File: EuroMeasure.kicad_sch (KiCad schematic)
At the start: 47 parts, among them SW1 RESET, SW2 ADR, U1 AMS1117-3.3, U2 STM32G030CxT, Y1 NX2520 16MHz

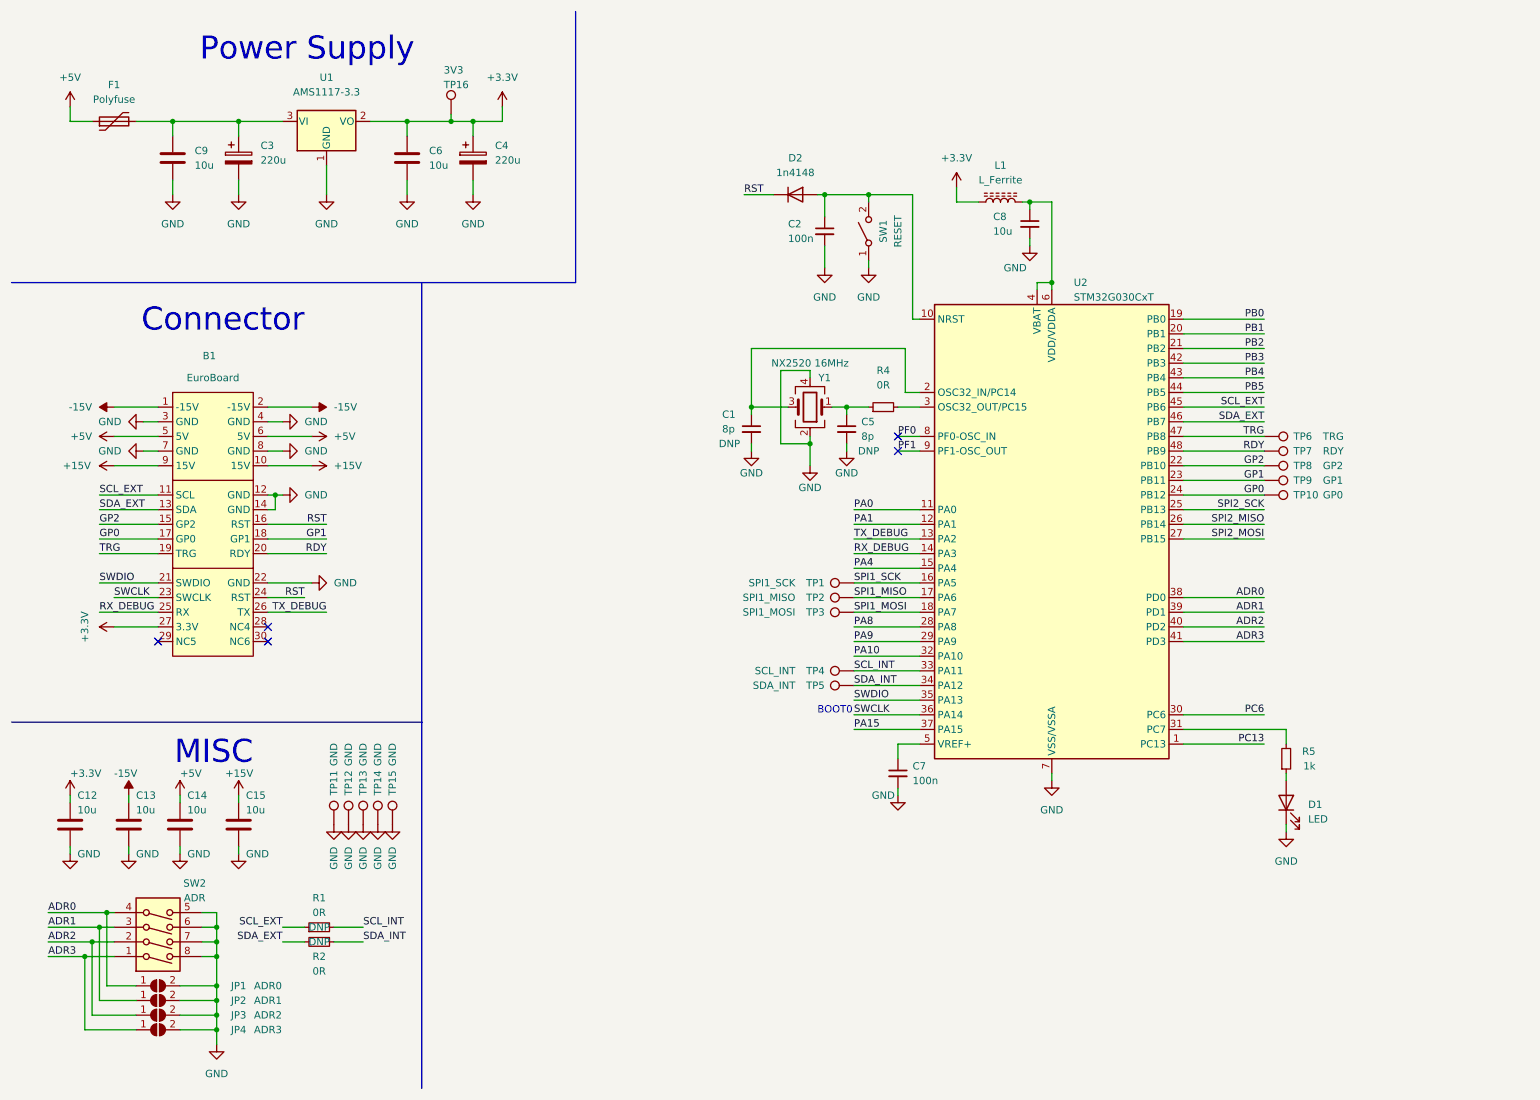
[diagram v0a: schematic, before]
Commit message: Fixed xtal connection
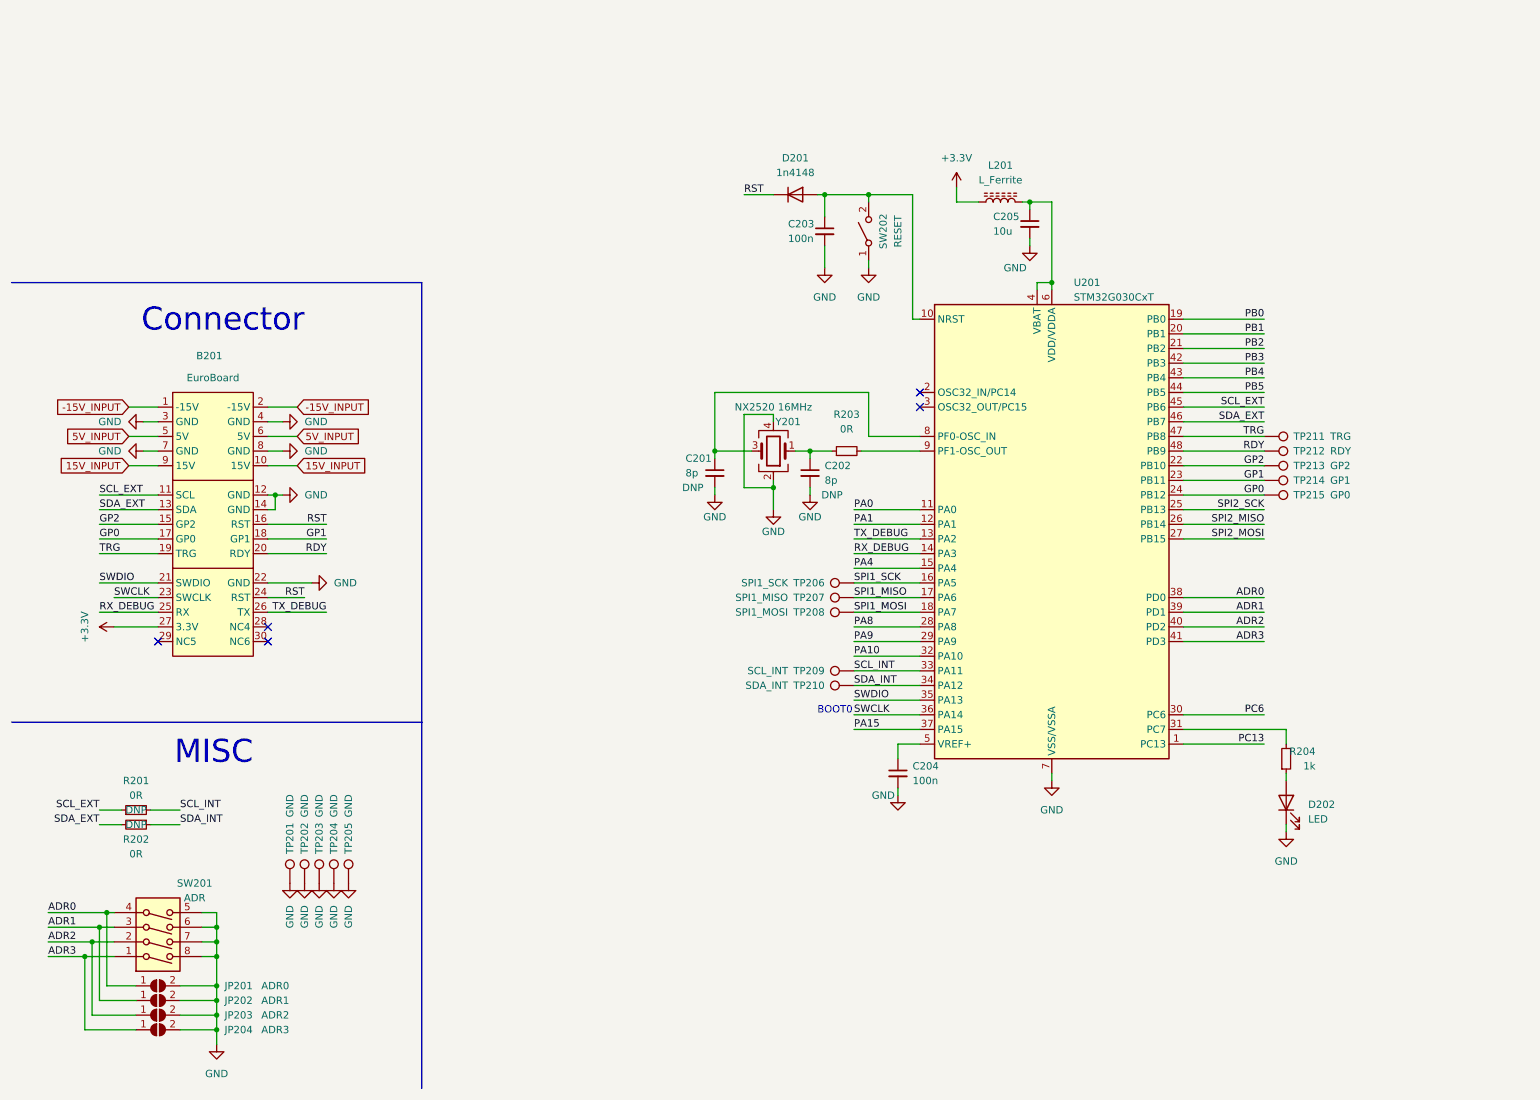
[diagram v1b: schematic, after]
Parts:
- removed C12, C13, C14, C15, C6, C9: 10u, Capacitor_SMD:C_0805_2012Metric_Pad1.18x1.45mm_HandSolder, symbol Device:C
- removed C3, C4: 220u, Capacitor_SMD:CP_Elec_6.3x7.7, symbol Device:C_Polarized
- removed F1: Polyfuse, Fuse:Fuse_1210_3225Metric, symbol Device:Polyfuse
- removed TP16: 3V3, MEMS_Custom:TestPoint_Pad_D1.0mm, symbol Connector:TestPoint
- removed U1: AMS1117-3.3, Package_TO_SOT_SMD:SOT-223-3_TabPin2, symbol Regulator_Linear:AMS1117-3.3
- renumbered B1 to B201, C1 to C201, C5 to C202, C2 to C203, C7 to C204, C8 to C205, D2 to D201, D1 to D202, JP1 to JP201, JP2 to JP202, JP3 to JP203, JP4 to JP204, L1 to L201, R1 to R201, R2 to R202, R4 to R203, R5 to R204, SW2 to SW201, SW1 to SW202, TP11 to TP201, TP12 to TP202, TP13 to TP203, TP14 to TP204, TP15 to TP205, TP1 to TP206, TP2 to TP207, TP3 to TP208, TP4 to TP209, TP5 to TP210, TP6 to TP211, TP7 to TP212, TP8 to TP213, TP9 to TP214, TP10 to TP215, U2 to U201, Y1 to Y201
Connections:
- net PF0 is gone; now on an unnamed net: U201.8 (PF0-OSC_IN)
- net at C201.1, Y201.3: no longer U201.2 (OSC32_IN/PC14)
- net at U201.3 (OSC32_OUT/PC15): no longer R203.2
- net +15V renamed 15V_INPUT
- net +5V renamed 5V_INPUT
- net -15V renamed -15V_INPUT
- net PF1: no longer names the net of U201.9 (PF1-OSC_OUT)
- net PF1: now also R203.2
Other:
- note removed: "Power Supply"
- moved on the sheet: C201, C202, R201, R202, R203, TP201, TP202, TP203, TP204, TP205, Y201

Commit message: Fixed programmer reset
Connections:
- net RST: no longer B201.24 (RST)
- net LOCAL_RST: now reaches C203.1, D201.2 (A), SW202.2 (B), U201.10 (NRST)
- net LOCAL_RST: now also B201.24 (RST)

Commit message: Updated euroboard footprint to accept lockout
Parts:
- TP213: value GP2 -> ~{LOCKOUT}
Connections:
- net GP2 renamed ~{LOCKOUT}
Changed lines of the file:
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@@
     (effects (font (size 1.27 1.27)) (justify left bottom))
   )
-  (label "GP2" (at 26.67 100.33 0) (fields_autoplaced)
+  (label "~{LOCKOUT}" (at 26.67 100.33 0) (fields_autoplaced)
     (effects (font (size 1.27 1.27)) (justify left bottom))
   )
@@
     (effects (font (size 1.27 1.27)) (justify right bottom))
   )
-  (label "GP2" (at 228.6 90.17 180) (fields_autoplaced)
+  (label "~{LOCKOUT}" (at 228.6 90.17 180) (fields_autoplaced)
     (effects (font (size 1.27 1.27)) (justify right bottom))
   )
@@
       (effects (font (size 1.27 1.27)) (justify left))
     )
-    (property "Value" "GP2" (at 240.03 90.17 90)
-      (effects (font (size 1.27 1.27)) (justify left))
-    )
+    (property "Value" "~{LOCKOUT}" (at 240.03 90.17 90)
+      (effects (font (size 1.27 1.27)) (justify left))
+    )

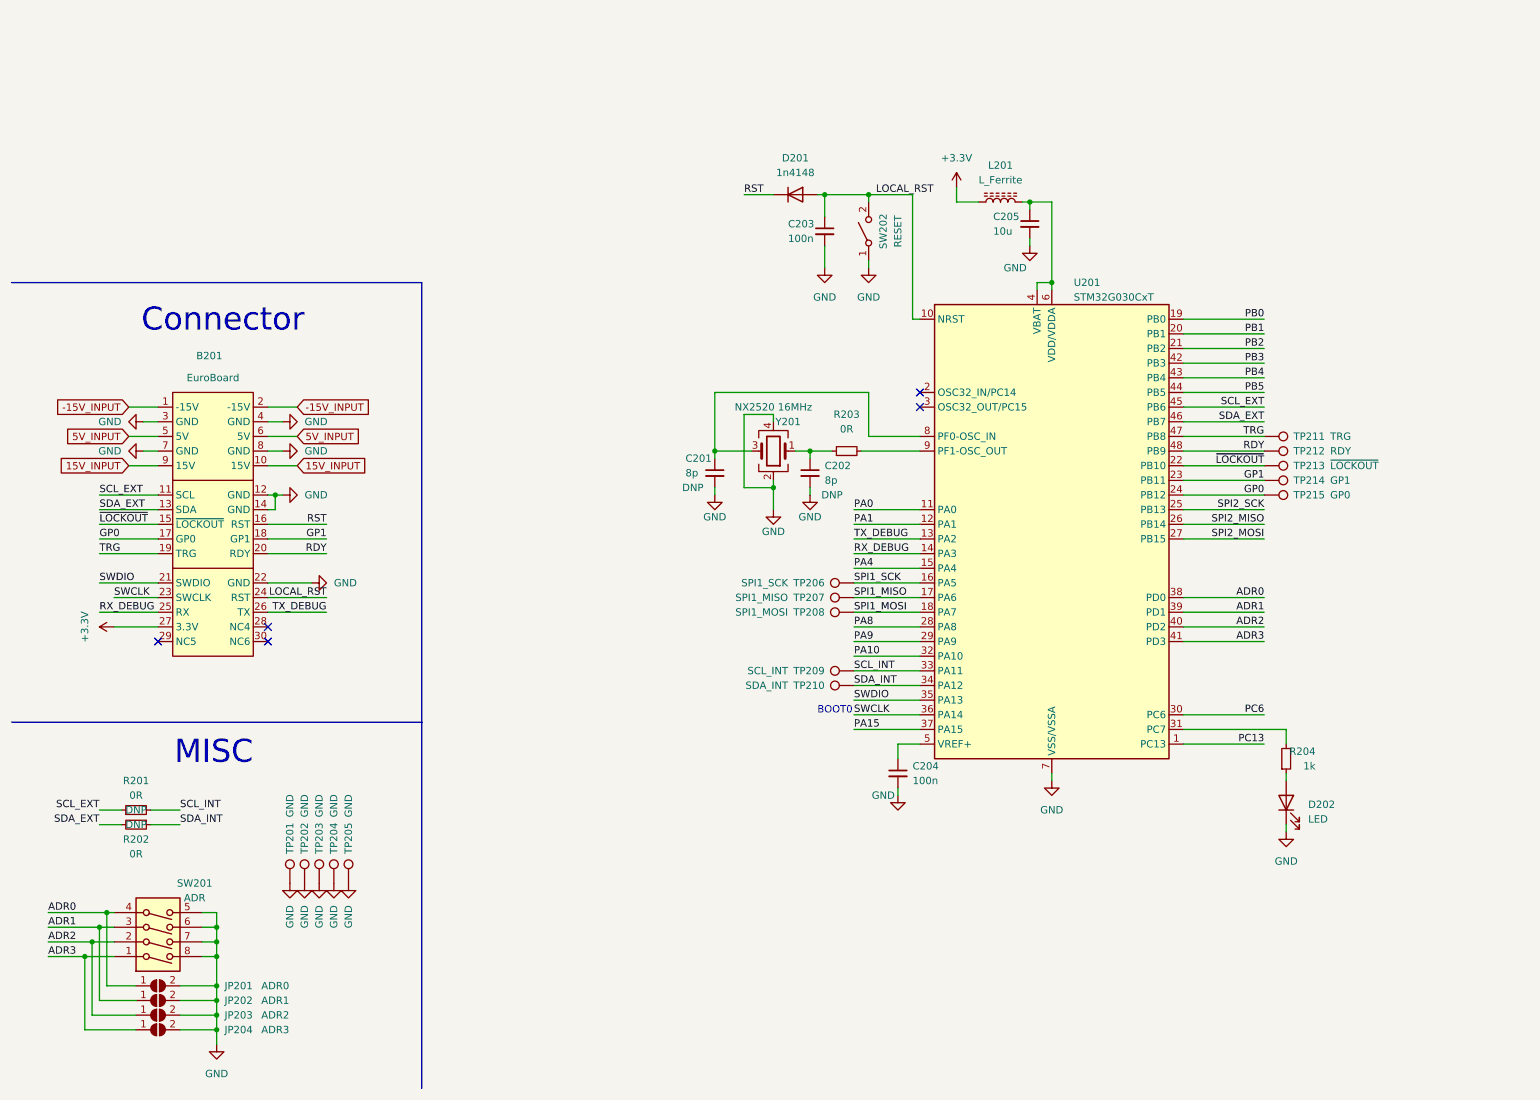
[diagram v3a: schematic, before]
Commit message: Converted for use as the single EuroMeasure.sch file
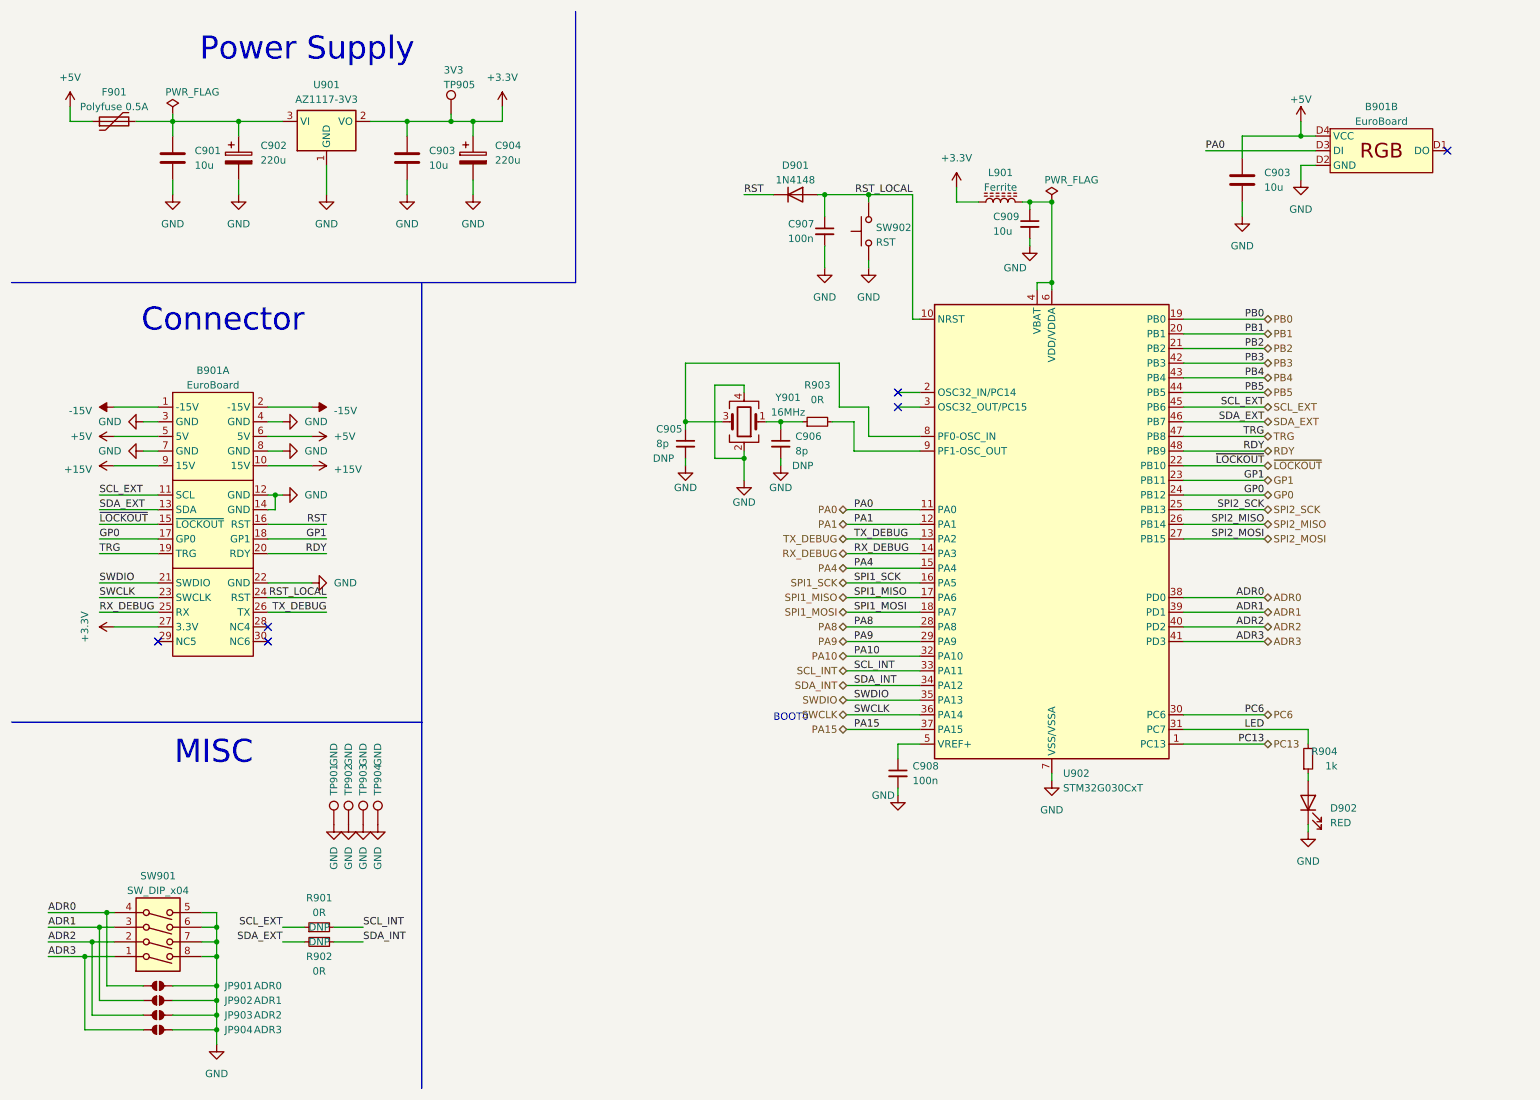
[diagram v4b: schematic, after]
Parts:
- removed B201: EuroBoard, MEMS_Custom:EuroMeasure, symbol MEMS_Custom:EuroBoard
- removed C201, C202: 8p, Capacitor_SMD:C_0805_2012Metric_Pad1.18x1.45mm_HandSolder, symbol Device:C_Small
- removed C203, C204: 100n, Capacitor_SMD:C_0805_2012Metric_Pad1.18x1.45mm_HandSolder, symbol Device:C_Small
- removed C205: 10u, Capacitor_SMD:C_0805_2012Metric_Pad1.18x1.45mm_HandSolder, symbol Device:C_Small
- removed D201: 1n4148, Diode_SMD:D_SOD-123, symbol Device:D
- removed D202: LED, LED_SMD:LED_0805_2012Metric_Pad1.15x1.40mm_HandSolder, symbol Device:LED
- removed JP201: ADR0, MEMS_Passive:R_0805_2012Metric_Jumper, symbol Jumper:SolderJumper_2_Open
- removed JP202: ADR1, MEMS_Passive:R_0805_2012Metric_Jumper, symbol Jumper:SolderJumper_2_Open
- removed JP203: ADR2, MEMS_Passive:R_0805_2012Metric_Jumper, symbol Jumper:SolderJumper_2_Open
- removed JP204: ADR3, MEMS_Passive:R_0805_2012Metric_Jumper, symbol Jumper:SolderJumper_2_Open
- removed L201: L_Ferrite, Inductor_SMD:L_0805_2012Metric_Pad1.15x1.40mm_HandSolder, symbol Device:L_Ferrite
- removed R201, R202, R203: 0R, Capacitor_SMD:C_0805_2012Metric_Pad1.18x1.45mm_HandSolder, symbol Device:R_Small
- removed R204: 1k, Resistor_SMD:R_0805_2012Metric_Pad1.20x1.40mm_HandSolder, symbol Device:R_Small
- removed SW201: ADR, Button_Switch_SMD:SW_DIP_SPSTx04_Slide_Omron_A6H-4101_W6.15mm_P1.27mm, symbol Switch:SW_DIP_x04
- removed SW202: RESET, Button_Switch_SMD:SW_SPST_B3S-1000, symbol Switch:SW_SPST
- removed TP201, TP202, TP203, TP204, TP205: GND, MEMS_Custom:TestPoint_Pad_D1.0mm, symbol Connector:TestPoint
- removed TP206: SPI1_SCK, MEMS_Custom:TestPoint_Pad_D1.0mm, symbol Connector:TestPoint
- removed TP207: SPI1_MISO, MEMS_Custom:TestPoint_Pad_D1.0mm, symbol Connector:TestPoint
- removed TP208: SPI1_MOSI, MEMS_Custom:TestPoint_Pad_D1.0mm, symbol Connector:TestPoint
- removed TP209: SCL_INT, MEMS_Custom:TestPoint_Pad_D1.0mm, symbol Connector:TestPoint
- removed TP210: SDA_INT, MEMS_Custom:TestPoint_Pad_D1.0mm, symbol Connector:TestPoint
- removed TP211: TRG, MEMS_Custom:TestPoint_Pad_D1.0mm, symbol Connector:TestPoint
- removed TP212: RDY, MEMS_Custom:TestPoint_Pad_D1.0mm, symbol Connector:TestPoint
- removed TP213: ~{LOCKOUT}, MEMS_Custom:TestPoint_Pad_D1.0mm, symbol Connector:TestPoint
- removed TP214: GP1, MEMS_Custom:TestPoint_Pad_D1.0mm, symbol Connector:TestPoint
- removed TP215: GP0, MEMS_Custom:TestPoint_Pad_D1.0mm, symbol Connector:TestPoint
- removed U201: STM32G030CxT, Package_QFP:LQFP-48_7x7mm_P0.5mm, symbol MEMS_IC:STM32G030CxT
- removed Y201: NX2520 16MHz, Oscillator:Oscillator_SMD_Abracon_ASDMB-4Pin_2.5x2.0mm, symbol Device:Crystal_GND24
- added B901: EuroBoard, MEMS_Custom:EuroMeasureLED, symbol MEMS_Custom:EuroBoardLED
- added C901, C903 (x2): 10u, Capacitor_SMD:C_0805_2012Metric_Pad1.18x1.45mm_HandSolder, symbol Device:C
- added C902, C904: 220u, Capacitor_SMD:CP_Elec_6.3x7.7, symbol Device:C_Polarized
- added C905, C906: 8p, Capacitor_SMD:C_0805_2012Metric_Pad1.18x1.45mm_HandSolder, symbol Device:C_Small
- added C907, C908: 100n, Capacitor_SMD:C_0805_2012Metric_Pad1.18x1.45mm_HandSolder, symbol Device:C_Small
- added C909: 10u, Capacitor_SMD:C_0805_2012Metric_Pad1.18x1.45mm_HandSolder, symbol Device:C_Small
- added D901: 1N4148, Diode_SMD:D_SOD-323F, symbol MEMS_Discrete-semiconductor:D_1N4148WS-SOD323
- added D902: RED, LED_SMD:LED_0805_2012Metric_Pad1.15x1.40mm_HandSolder, symbol MEMS_Discrete-semiconductor:LED_0805_Red
- added F901: Polyfuse 0.5A, Fuse:Fuse_1210_3225Metric, symbol MEMS_Protection:Polyfuse-500mA-1206L050/15YR
- added JP901: ADR0, MEMS_Passive:R_0805_2012Metric_Jumper, symbol MEMS_Passive:SolderableJumper
- added JP902: ADR1, MEMS_Passive:R_0805_2012Metric_Jumper, symbol MEMS_Passive:SolderableJumper
- added JP903: ADR2, MEMS_Passive:R_0805_2012Metric_Jumper, symbol MEMS_Passive:SolderableJumper
- added JP904: ADR3, MEMS_Passive:R_0805_2012Metric_Jumper, symbol MEMS_Passive:SolderableJumper
- added L901: Ferrite, Inductor_SMD:L_0805_2012Metric_Pad1.15x1.40mm_HandSolder, symbol MEMS_Passive:L_Ferrite_742792040
- added R901, R902, R903: 0R, Capacitor_SMD:C_0805_2012Metric_Pad1.18x1.45mm_HandSolder, symbol Device:R_Small
- added R904: 1k, Resistor_SMD:R_0805_2012Metric_Pad1.20x1.40mm_HandSolder, symbol Device:R_Small
- added SW901: SW_DIP_x04, Button_Switch_SMD:SW_DIP_SPSTx04_Slide_Omron_A6H-4101_W6.15mm_P1.27mm, symbol MEMS_Electromechanical:SW_DIP_A6H-4101
- added SW902: RST, Button_Switch_SMD:SW_SPST_B3S-1000, symbol MEMS_Electromechanical:SW_Push_Tact_B3S-1000
- added TP901, TP902, TP903, TP904: GND, MEMS_Custom:TestPoint_Pad_D1.0mm, symbol Connector:TestPoint
- added TP905: 3V3, MEMS_Custom:TestPoint_Pad_D1.0mm, symbol Connector:TestPoint
- added U901: AZ1117-3V3, Package_TO_SOT_SMD:SOT-223-3_TabPin2, symbol MEMS_IC:AZ1117IH-3.3TRG1-SOT223
- added U902: STM32G030CxT, Package_QFP:LQFP-48_7x7mm_P0.5mm, symbol MEMS_IC:STM32G030CxT
- added Y901: 16MHz, Oscillator:Oscillator_SMD_Abracon_ASDMB-4Pin_2.5x2.0mm, symbol MEMS_Passive:Crystal_16MHz_ECS-160-8-36CKM-TR3
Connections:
- net +3.3V: now also B901.27 (3.3V), C903.1, C904.1, L901.1, TP905.1, U901.2 (VO)
- net ADR0: now also JP901.1, SW901.4, U902.38 (PD0)
- net ADR1: now also JP902.1, SW901.3, U902.39 (PD1)
- net ADR2: now also JP903.1, SW901.2, U902.40 (PD2)
- net ADR3: now also JP904.1, SW901.1, U902.41 (PD3)
- net GND: now also B901.12 (GND), B901.14 (GND), B901.22 (GND), B901.3 (GND), B901.4 (GND), B901.7 (GND), B901.8 (GND), B901.D2 (GND), C901.2, C902.2, C903.2, C903.2, C904.2, C905.2, C906.2, C907.2, C908.2, C909.2, D902.1 (K), JP901.2, JP902.2, JP903.2, JP904.2, SW901.5, SW901.6, SW901.7, SW901.8, SW902.1, TP901.1, TP902.1, TP903.1, TP904.1, U901.1 (GND), U902.7 (VSS/VSSA), Y901.2, Y901.4
- net GP0: now also B901.17 (GP0), U902.24 (PB12)
- net GP1: now also B901.18 (GP1), U902.23 (PB11)
- net PA0: now also B901.D3 (DI), U902.11 (PA0)
- net PA1: now also U902.12 (PA1)
- net PA10: now also U902.32 (PA10)
- net PA15: now also U902.37 (PA15)
- net PA4: now also U902.15 (PA4)
- net PA8: now also U902.28 (PA8)
- net PA9: now also U902.29 (PA9)
- net PB0: now also U902.19 (PB0)
- net PB1: now also U902.20 (PB1)
- net PB2: now also U902.21 (PB2)
- net PB3: now also U902.42 (PB3)
- net PB4: now also U902.43 (PB4)
- net PB5: now also U902.44 (PB5)
- net PC13: now also U902.1 (PC13)
- net PC6: now also U902.30 (PC6)
- net RDY: now also B901.20 (RDY), U902.48 (PB9)
- net RST: now also B901.16 (RST), D901.1 (K)
- net RX_DEBUG: now also B901.25 (RX), U902.14 (PA3)
- net SCL_EXT: now also B901.11 (SCL), R901.1, U902.45 (PB6)
- net SCL_INT: now also R901.2, U902.33 (PA11)
- net SDA_EXT: now also B901.13 (SDA), R902.2, U902.46 (PB7)
- net SDA_INT: now also R902.1, U902.34 (PA12)
- net SPI1_MISO: now also U902.17 (PA6)
- net SPI1_MOSI: now also U902.18 (PA7)
- net SPI1_SCK: now also U902.16 (PA5)
- net SPI2_MISO: now also U902.26 (PB14)
- net SPI2_MOSI: now also U902.27 (PB15)
- net SPI2_SCK: now also U902.25 (PB13)
- net SWCLK: now also B901.23 (SWCLK), U902.36 (PA14)
- net SWDIO: now also B901.21 (SWDIO), U902.35 (PA13)
- net TRG: now also B901.19 (TRG), U902.47 (PB8)
- net TX_DEBUG: now also B901.26 (TX), U902.13 (PA2)
- net ~{LOCKOUT}: now also B901.15 (~{LOCKOUT}), U902.22 (PB10)
- new net: C909.1, L901.2, U902.4 (VBAT), U902.6 (VDD/VDDA)
- new net: C906.1, R903.1, Y901.1
- new net: C905.1, U902.8 (PF0-OSC_IN), Y901.3
- new net: C901.1, C902.1, F901.2, U901.3 (VI)
- new net: D902.2 (A), R904.1
- new net: R903.2, U902.9 (PF1-OSC_OUT)
- new net: C908.1, U902.5 (VREF+)
- new net +15V: B901.10 (15V), B901.9 (15V)
- new net +5V: B901.5 (5V), B901.6 (5V), B901.D4 (VCC), C903.1, F901.1
- new net -15V: B901.1 (-15V), B901.2 (-15V)
- new net LED: R904.2, U902.31 (PC7)
- new net RST_LOCAL: B901.24 (RST), C907.1, D901.2 (A), SW902.2, U902.10 (NRST)
- no-connect marks 5 -> 6
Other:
- note added: "Power Supply"
- title: EuroMeasure-Module -> (none)
